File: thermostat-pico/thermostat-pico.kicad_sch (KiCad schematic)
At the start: 24 parts, among them J1 VAC IN, J2 CTRL, J3 UART, U1 LY68L6400SLIT, U2 ESP32-PICO-D4, U3 LM358DR2G, U4 TPS5430DDA, U5 TPS5430DDA

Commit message: Should be finished
Maybe the antenna could be different
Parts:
- removed AE1: Antenna, RF_Antenna:Texas_SWRA117D_2.4GHz_Right, symbol Device:Antenna
- removed C4: 0.1uF/50V, Capacitor_SMD:C_0603_1608Metric, symbol Device:C_Small
- added AE1: Antenna_Shield, RF_Antenna:Texas_SWRA117D_2.4GHz_Left, symbol Device:Antenna_Shield
- added C10: 0.01uF, Capacitor_SMD:C_0402_1005Metric, symbol Device:C_Small
- added C8, C9: 470uF/6.3V, Capacitor_Tantalum_SMD:CP_EIA-7343-31_Kemet-D, symbol Device:C_Small
- added D3: SS34, Diode_SMD:D_SMA, symbol Device:D_Schottky_Small
- added H1, H2: MountingHole_Pad, symbol Mechanical:MountingHole_Pad
- added L2: 22uH, inductors:L_SXN_SMRH74-220MT, symbol Device:L_Small
- added R10: 270, Resistor_SMD:R_0603_1608Metric, symbol Device:R_Small
- added R5, R6: 10k, Resistor_SMD:R_0603_1608Metric, symbol Device:R_Small
- added R7: 1.1k, Resistor_SMD:R_0603_1608Metric, symbol Device:R_Small
- added R8: 5.6k, Resistor_SMD:R_0603_1608Metric, symbol Device:R_Small
- added R9: 33, Resistor_SMD:R_0603_1608Metric, symbol Device:R_Small
- C3: value 0.1uF/50V -> 0.1uF; footprint Capacitor_SMD:C_0603_1608Metric -> Capacitor_SMD:C_0402_1005Metric
- C7: value 0.01uF -> 0.1uF
- L1: renamed from L?; value 10uH/50V -> 22uH; footprint (none) -> inductors:L_SXN_SMRH74-220MT
- gave numbers to parts that had none: 1
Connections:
- net GND: now also C3.1, JP1.2 (B), U3.4 (V-), AE1.2 (Shield), C10.2, C8.2, C9.2, D3.2 (A), H1.1, H2.1, R10.1, R9.1; no longer C3.2
- net VCC33: now also U2.1 (VDDA), U2.19 (VDD3P3_RTC), U2.3 (VDDA3P3), U2.37 (VDD3P3_CPU), U2.4 (VDDA3P3), U2.43 (VDDA), U2.46 (VDDA), C10.1, C8.1, R6.1
- net PH12: now reaches C5.2, U4.8 (PH)
- net PH12: now also D3.1 (K), L2.1
- net at U2.2 (LNA_IN): now also AE1.1 (A)
- net PH33: now reaches C6.2, D2.1 (K), L1.1, U5.8 (PH)
- net VCC12: now reaches U3.8 (V+)
- net VCC12: now also C9.1, L2.2, R5.1
- net ADC1: now reaches R3.2, R4.1
- net ADC1: now also C3.2, U2.5 (SENSOR_VP)
- net DAC1: now reaches U3.3 (+)
- net DAC1: now also U2.14 (IO25)
- net at U5.4 (VSENSE): now also R6.2, R8.2
- net DAC2: now reaches U2.15 (IO26)
- net BOOT: now reaches U2.23 (IO0)
- net BOOT: now also JP1.1 (A)
- net ADC2: now reaches U2.6 (SENSOR_CAPP)
- net at U4.4 (VSENSE): now also R5.2, R7.2
- net REC_OUT renamed D1_OUT
- net D1_OUT: no longer C3.1
- new net: R10.2, R8.1
- new net: R7.1, R9.2
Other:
- note added: "TODO: Choose some sensible connectors (that are small) and don't need to be cassellated"
- note added: "V_{ref} = 1.221 V"
- note added: "hook up slow start"
- note removed: "Choose some sensible connectors (that are small)"

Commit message: Added slow start circuit
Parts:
- added C4: 1uF/5V, Capacitor_SMD:C_0402_1005Metric, symbol Device:C_Polarized_Small
- added R11: 10k, Resistor_SMD:R_0201_0603Metric, symbol Device:R_Small
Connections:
- net GND: now also C4.2
- net VCC33: now also R11.1
- net CHIP_PU: now reaches U2.9 (EN)
- net CHIP_PU: now also C4.1, R11.2
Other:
- note added: "Power up delay (RC=10ms)"
- note added: "TODO: hook up slow start"
- note added: "alternatively use a 3216 ANT3216LL00R2400A"
- note removed: "TODO: Choose some sensible connectors (that are small) and don't need to be cassellated"
- note removed: "hook up slow start"
- moved on the sheet: H1, H2

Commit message: Add more connectors
And use a bigger op-amp. Surprised this fit.
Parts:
- removed U3: LM358DR2G, Package_SO:SOIC-8_3.9x4.9mm_P1.27mm, symbol Amplifier_Operational:LM358
- added C11: 0.1uF, Capacitor_SMD:C_0402_1005Metric, symbol Device:C_Small
- added R12: 33k, Resistor_SMD:R_0201_0603Metric, symbol Device:R_Small
- added R13: 68k, Resistor_SMD:R_0201_0603Metric, symbol Device:R_Small
- added R14: 18k, Resistor_SMD:R_0201_0603Metric, symbol Device:R_Small
- added R15: 2k, Resistor_SMD:R_0201_0603Metric, symbol Device:R_Small
- added U6: LM324DT, Package_SO:SOIC-14_3.9x8.7mm_P1.27mm, symbol Amplifier_Operational:LM324
- H1, H2: footprint (none) -> MountingHole:MountingHole_2.2mm_M2_DIN965_Pad
- J2: value CTRL -> Conn_01x06; footprint Connector_JST:JST_XH_B4B-XH-A_1x04_P2.50mm_Vertical -> Connector_JST:JST_XH_B6B-XH-A_1x06_P2.50mm_Vertical; symbol Connector_Generic:Conn_01x04 -> Connector_Generic:Conn_01x06
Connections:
- net CTRL0_IN is gone; now on net VCC33: J2.2 (Pin_2)
- net ADC2: now also C11.2, R14.2, R15.1
- net DAC1: now also U6.3 (+)
- net DAC2: now also U6.5 (+)
- net GND: now also C11.1, R12.2, R15.2, U6.11 (V-)
- net VCC12: now also U6.4 (V+)
- net at R1.1, R2.1: now also U6.2 (-)
- net at R3.1: now also U6.8, U6.9 (-)
- net CTRL2_IN: now reaches J2.4 (Pin_4)
- net CTRL2_IN: now also U6.12 (+)
- net CTRL0_OUT renamed CTRL1_IN
- net CTRL1_IN: now also U6.10 (+); no longer R2.2
- new net: R14.1, U6.13 (-), U6.14
- new net: R12.1, R13.1, U6.6 (-)
- new net CTRL1_OUT: J2.5 (Pin_5), R2.2, U6.1
- new net CTRL2_OUT: J2.6 (Pin_6), R13.2, U6.7
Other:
- note removed: "TODO: hook up slow start"
- moved on the sheet: C1, C2, C3, C4, C5, C6, C8, C9, D1, D2, D3, H1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

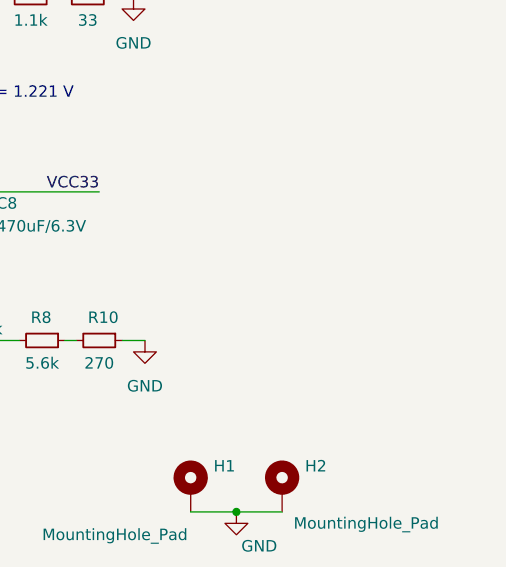
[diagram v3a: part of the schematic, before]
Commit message: Assembly updates
Apparently they can't do 0201 and need tooling holes
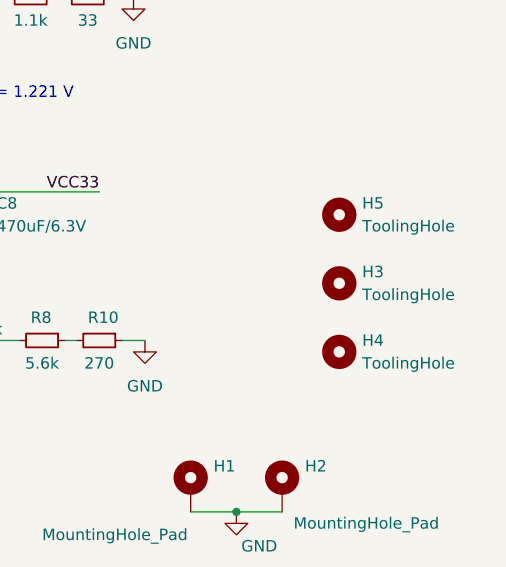
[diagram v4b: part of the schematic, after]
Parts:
- added H3, H4, H5: ToolingHole, kelvie:ToolingHole_1.152mm, symbol Mechanical:MountingHole
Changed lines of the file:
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@@
     (pin "1")
+  )
+  (symbol (lib_id "Mechanical:MountingHole") (at 252.73 142.24 0) (unit 1)
+    (in_bom yes) (on_board yes) (fields_autoplaced)
+    (property "Reference" "H3" (id 0) (at 255.27 140.9699 0)
+      (effects (font (size 1.27 1.27)) (justify left))
+    )
+    (property "Value" "ToolingHole" (id 1) (at 255.27 143.5099 0)
+      (effects (font (size 1.27 1.27)) (justify left))
+    )
+    (property "Footprint" "kelvie:ToolingHole_1.152mm" (id 2) (at 252.73 142.24 0)
+      (effects (font (size 1.27 1.27)) hide)
+    )
+    (property "Datasheet" "~" (id 3) (at 252.73 142.24 0)
+      (effects (font (size 1.27 1.27)) hide)
+    )
   )
   (symbol (lib_id "Device:C_Small") (at 157.48 134.62 0) (unit 1)
@@
     (pin "2")
   )
+  (symbol (lib_id "Mechanical:MountingHole") (at 252.73 149.86 0) (unit 1)
+    (in_bom yes) (on_board yes) (fields_autoplaced)
+    (property "Reference" "H4" (id 0) (at 255.27 148.5899 0)
+      (effects (font (size 1.27 1.27)) (justify left))
+    )
+    (property "Value" "ToolingHole" (id 1) (at 255.27 151.1299 0)
+      (effects (font (size 1.27 1.27)) (justify left))
+    )
+    (property "Footprint" "kelvie:ToolingHole_1.152mm" (id 2) (at 252.73 149.86 0)
+      (effects (font (size 1.27 1.27)) hide)
+    )
+    (property "Datasheet" "~" (id 3) (at 252.73 149.86 0)
+      (effects (font (size 1.27 1.27)) hide)
+    )
+  )
   (symbol (lib_id "Device:R_Small") (at 208.28 107.95 0) (unit 1)
     (in_bom yes) (on_board yes)
@@
     (pin "1")
   )
+  (symbol (lib_id "Mechanical:MountingHole") (at 252.73 134.62 0) (unit 1)
+    (in_bom yes) (on_board yes) (fields_autoplaced)
+    (property "Reference" "H5" (id 0) (at 255.27 133.3499 0)
+      (effects (font (size 1.27 1.27)) (justify left))
+    )
+    (property "Value" "ToolingHole" (id 1) (at 255.27 135.8899 0)
+      (effects (font (size 1.27 1.27)) (justify left))
+    )
+    (property "Footprint" "kelvie:ToolingHole_1.152mm" (id 2) (at 252.73 134.62 0)
+      (effects (font (size 1.27 1.27)) hide)
+    )
+    (property "Datasheet" "~" (id 3) (at 252.73 134.62 0)
+      (effects (font (size 1.27 1.27)) hide)
+    )
+  )
   (symbol (lib_id "power:GND") (at 176.53 149.86 0) (unit 1)
     (in_bom yes) (on_board yes) (fields_autoplaced)
@@
       (reference "H2") (unit 1) (value "MountingHole_Pad") (footprint "MountingHole:MountingHole_2.2mm_M2_DIN965_Pad")
     )
+    (path "/9ef5e703-a32f-4d55-916d-f0b78eccaca2"
+      (reference "H3") (unit 1) (value "ToolingHole") (footprint "kelvie:ToolingHole_1.152mm")
+    )
+    (path "/d3db0faf-24c3-4e5e-a21a-0038deb82e7a"
+      (reference "H4") (unit 1) (value "ToolingHole") (footprint "kelvie:ToolingHole_1.152mm")
+    )
+    (path "/d9e05401-8962-4c00-81aa-5faf29ebaf63"
+      (reference "H5") (unit 1) (value "ToolingHole") (footprint "kelvie:ToolingHole_1.152mm")
+    )
     (path "/f1534488-0c57-4f37-9331-650460480fa5"

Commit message: Update schematic as well
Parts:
- R1, R11, R12, R13, R14, R15, R2, R3, R4: footprint Resistor_SMD:R_0201_0603Metric -> Resistor_SMD:R_0402_1005Metric
- R10, R5, R6, R7, R8, R9: footprint Resistor_SMD:R_0603_1608Metric -> Resistor_SMD:R_0402_1005Metric
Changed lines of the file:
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@@
     (property "Reference" "R2" (id 0) (at 154.94 36.83 90))
     (property "Value" "68k" (id 1) (at 154.94 39.37 90))
-    (property "Footprint" "Resistor_SMD:R_0201_0603Metric" (id 2) (at 154.94 34.29 0)
+    (property "Footprint" "Resistor_SMD:R_0402_1005Metric" (id 2) (at 154.94 34.29 0)
       (effects (font (size 1.27 1.27)) hide)
     )
@@
     (property "Reference" "R3" (id 0) (at 213.36 29.21 90))
     (property "Value" "18k" (id 1) (at 213.36 31.75 90))
-    (property "Footprint" "Resistor_SMD:R_0201_0603Metric" (id 2) (at 213.36 26.67 0)
+    (property "Footprint" "Resistor_SMD:R_0402_1005Metric" (id 2) (at 213.36 26.67 0)
       (effects (font (size 1.27 1.27)) hide)
     )
@@
       (effects (font (size 1.27 1.27)) (justify left))
     )
-    (property "Footprint" "Resistor_SMD:R_0201_0603Metric" (id 2) (at 142.24 73.66 0)
+    (property "Footprint" "Resistor_SMD:R_0402_1005Metric" (id 2) (at 142.24 73.66 0)
       (effects (font (size 1.27 1.27)) hide)
     )
@@
     )
     (property "Value" "5.6k" (id 1) (at 219.71 151.13 90))
-    (property "Footprint" "Resistor_SMD:R_0603_1608Metric" (id 2) (at 219.71 148.59 0)
+    (property "Footprint" "Resistor_SMD:R_0402_1005Metric" (id 2) (at 219.71 148.59 0)
       (effects (font (size 1.27 1.27)) hide)
     )
@@
       (effects (font (size 1.27 1.27)) (justify left))
     )
-    (property "Footprint" "Resistor_SMD:R_0201_0603Metric" (id 2) (at 90.17 140.97 0)
+    (property "Footprint" "Resistor_SMD:R_0402_1005Metric" (id 2) (at 90.17 140.97 0)
       (effects (font (size 1.27 1.27)) hide)
     )
@@
     )
     (property "Value" "270" (id 1) (at 226.06 151.13 90))
-    (property "Footprint" "Resistor_SMD:R_0603_1608Metric" (id 2) (at 226.06 148.59 0)
+    (property "Footprint" "Resistor_SMD:R_0402_1005Metric" (id 2) (at 226.06 148.59 0)
       (effects (font (size 1.27 1.27)) hide)
     )
@@
       (effects (font (size 1.27 1.27)) (justify left))
     )
-    (property "Footprint" "Resistor_SMD:R_0201_0603Metric" (id 2) (at 142.24 36.83 0)
+    (property "Footprint" "Resistor_SMD:R_0402_1005Metric" (id 2) (at 142.24 36.83 0)
       (effects (font (size 1.27 1.27)) hide)
     )
@@
     (property "Reference" "R13" (id 0) (at 154.94 73.66 90))
     (property "Value" "68k" (id 1) (at 154.94 76.2 90))
-    (property "Footprint" "Resistor_SMD:R_0201_0603Metric" (id 2) (at 154.94 71.12 0)
+    (property "Footprint" "Resistor_SMD:R_0402_1005Metric" (id 2) (at 154.94 71.12 0)
       (effects (font (size 1.27 1.27)) hide)
     )
@@
       (effects (font (size 1.27 1.27)) (justify left))
     )
-    (property "Footprint" "Resistor_SMD:R_0201_0603Metric" (id 2) (at 217.17 69.85 0)
+    (property "Footprint" "Resistor_SMD:R_0402_1005Metric" (id 2) (at 217.17 69.85 0)
       (effects (font (size 1.27 1.27)) hide)
     )
@@
       (effects (font (size 1.27 1.27)) (justify left))
     )
-    (property "Footprint" "Resistor_SMD:R_0201_0603Metric" (id 2) (at 217.17 31.75 0)
+    (property "Footprint" "Resistor_SMD:R_0402_1005Metric" (id 2) (at 217.17 31.75 0)
       (effects (font (size 1.27 1.27)) hide)
     )
@@
       (effects (font (size 1.27 1.27)) (justify left))
     )
-    (property "Footprint" "Resistor_SMD:R_0603_1608Metric" (id 2) (at 209.55 146.05 0)
+    (property "Footprint" "Resistor_SMD:R_0402_1005Metric" (id 2) (at 209.55 146.05 0)
       (effects (font (size 1.27 1.27)) hide)
     )
@@
     (property "Reference" "R14" (id 0) (at 213.36 67.31 90))
     (property "Value" "18k" (id 1) (at 213.36 69.85 90))
-    (property "Footprint" "Resistor_SMD:R_0201_0603Metric" (id 2) (at 213.36 64.77 0)
+    (property "Footprint" "Resistor_SMD:R_0402_1005Metric" (id 2) (at 213.36 64.77 0)
       (effects (font (size 1.27 1.27)) hide)
     )
@@
       (effects (font (size 1.27 1.27)) (justify left))
     )
-    (property "Footprint" "Resistor_SMD:R_0603_1608Metric" (id 2) (at 208.28 107.95 0)
+    (property "Footprint" "Resistor_SMD:R_0402_1005Metric" (id 2) (at 208.28 107.95 0)
       (effects (font (size 1.27 1.27)) hide)
     )
@@
     )
     (property "Value" "33" (id 1) (at 224.79 113.03 90))
-    (property "Footprint" "Resistor_SMD:R_0603_1608Metric" (id 2) (at 224.79 110.49 0)
+    (property "Footprint" "Resistor_SMD:R_0402_1005Metric" (id 2) (at 224.79 110.49 0)
       (effects (font (size 1.27 1.27)) hide)
     )
@@
     )
     (property "Value" "1.1k" (id 1) (at 218.44 113.03 90))
-    (property "Footprint" "Resistor_SMD:R_0603_1608Metric" (id 2) (at 218.44 110.49 0)
+    (property "Footprint" "Resistor_SMD:R_0402_1005Metric" (id 2) (at 218.44 110.49 0)
       (effects (font (size 1.27 1.27)) hide)
     )
@@
     )
     (path "/72192ee1-be2c-437f-bdfe-9be8d8097e0f"
-      (reference "R1") (unit 1) (value "33k") (footprint "Resistor_SMD:R_0201_0603Metric")
+      (reference "R1") (unit 1) (value "33k") (footprint "Resistor_SMD:R_0402_1005Metric")
     )
     (path "/169daa4b-395e-4558-98b5-0efbe8759631"
-      (reference "R2") (unit 1) (value "68k") (footprint "Resistor_SMD:R_0201_0603Metric")
+      (reference "R2") (unit 1) (value "68k") (footprint "Resistor_SMD:R_0402_1005Metric")
     )
     (path "/3f6c54e3-4e0f-433c-b1f9-04b6aa3e12dd"
-      (reference "R3") (unit 1) (value "18k") (footprint "Resistor_SMD:R_0201_0603Metric")
+      (reference "R3") (unit 1) (value "18k") (footprint "Resistor_SMD:R_0402_1005Metric")
     )
     (path "/9a4d0ce7-7a9b-46f9-8212-69f5f5afa371"
-      (reference "R4") (unit 1) (value "2k") (footprint "Resistor_SMD:R_0201_0603Metric")
+      (reference "R4") (unit 1) (value "2k") (footprint "Resistor_SMD:R_0402_1005Metric")
     )
     (path "/d61d882f-0d79-4d83-8ab4-8a83798fa9b3"
-      (reference "R5") (unit 1) (value "10k") (footprint "Resistor_SMD:R_0603_1608Metric")
+      (reference "R5") (unit 1) (value "10k") (footprint "Resistor_SMD:R_0402_1005Metric")
     )
     (path "/b4f2e83a-e9ef-4b38-a257-58af2a7607a9"
-      (reference "R6") (unit 1) (value "10k") (footprint "Resistor_SMD:R_0603_1608Metric")
+      (reference "R6") (unit 1) (value "10k") (footprint "Resistor_SMD:R_0402_1005Metric")
     )
     (path "/fdb8b7c2-6e1f-4a83-b040-8708846811b1"
-      (reference "R7") (unit 1) (value "1.1k") (footprint "Resistor_SMD:R_0603_1608Metric")
+      (reference "R7") (unit 1) (value "1.1k") (footprint "Resistor_SMD:R_0402_1005Metric")
     )
     (path "/5451993e-97bd-4d4c-861e-f6e7918e6be0"
-      (reference "R8") (unit 1) (value "5.6k") (footprint "Resistor_SMD:R_0603_1608Metric")
+      (reference "R8") (unit 1) (value "5.6k") (footprint "Resistor_SMD:R_0402_1005Metric")
     )
     (path "/f21dba44-7a44-48a4-afbf-4047d3e6c830"
-      (reference "R9") (unit 1) (value "33") (footprint "Resistor_SMD:R_0603_1608Metric")
+      (reference "R9") (unit 1) (value "33") (footprint "Resistor_SMD:R_0402_1005Metric")
     )
     (path "/6bd494fc-986d-4d70-9437-eebba9103a7c"
-      (reference "R10") (unit 1) (value "270") (footprint "Resistor_SMD:R_0603_1608Metric")
+      (reference "R10") (unit 1) (value "270") (footprint "Resistor_SMD:R_0402_1005Metric")
     )
     (path "/64f8e5f8-4138-47db-b4da-baf8b055af40"
-      (reference "R11") (unit 1) (value "10k") (footprint "Resistor_SMD:R_0201_0603Metric")
+      (reference "R11") (unit 1) (value "10k") (footprint "Resistor_SMD:R_0402_1005Metric")
     )
     (path "/4f2f0167-ac23-4fd2-a2e7-3fe2c441e201"
-      (reference "R12") (unit 1) (value "33k") (footprint "Resistor_SMD:R_0201_0603Metric")
+      (reference "R12") (unit 1) (value "33k") (footprint "Resistor_SMD:R_0402_1005Metric")
     )
     (path "/7b9d005b-1d3e-4438-9d04-7952825419ed"
-      (reference "R13") (unit 1) (value "68k") (footprint "Resistor_SMD:R_0201_0603Metric")
+      (reference "R13") (unit 1) (value "68k") (footprint "Resistor_SMD:R_0402_1005Metric")
     )
     (path "/d216f59c-b3e8-41ae-bb1f-c0fc9f37cc31"
-      (reference "R14") (unit 1) (value "18k") (footprint "Resistor_SMD:R_0201_0603Metric")
+      (reference "R14") (unit 1) (value "18k") (footprint "Resistor_SMD:R_0402_1005Metric")
     )
     (path "/96248f25-b98a-46c4-9b58-a75fcbaf28ed"
-      (reference "R15") (unit 1) (value "2k") (footprint "Resistor_SMD:R_0201_0603Metric")
+      (reference "R15") (unit 1) (value "2k") (footprint "Resistor_SMD:R_0402_1005Metric")
     )
     (path "/7b13e11c-0fa5-46f4-acf2-567d5a57dcc2"
